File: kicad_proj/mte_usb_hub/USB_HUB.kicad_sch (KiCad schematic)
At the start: 50 parts

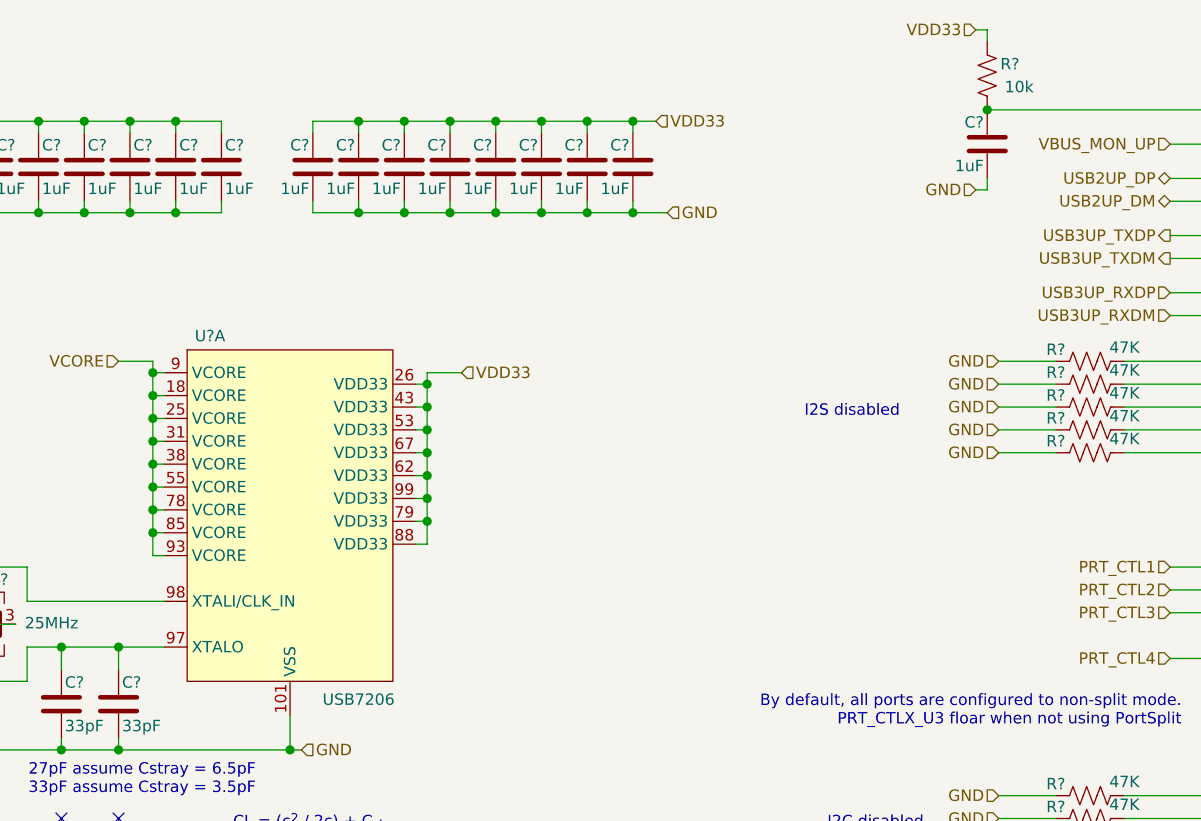
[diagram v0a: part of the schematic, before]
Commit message: Finishes upstream USB setup
No power setup, no downstream ports setup
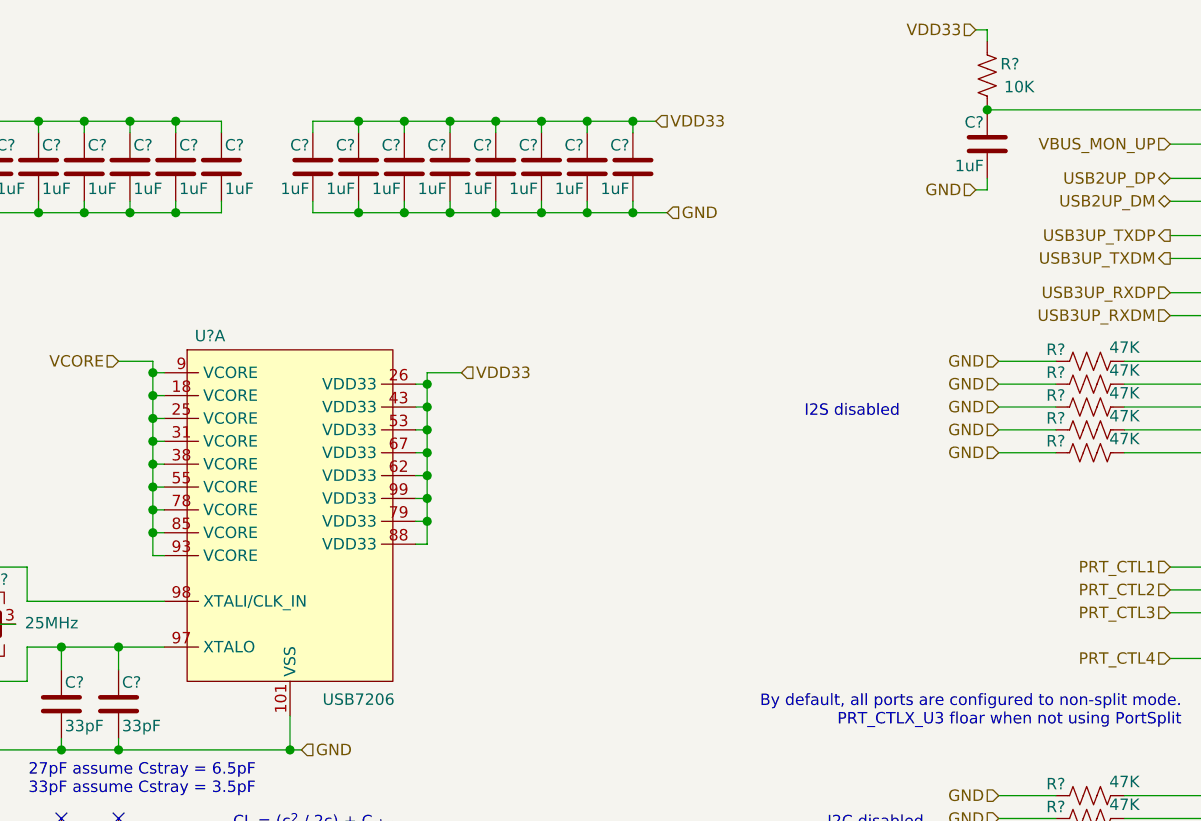
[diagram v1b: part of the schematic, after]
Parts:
- C? (x18): symbol capacitors:CC0402KRX5R7BB105 -> mte_usb_hub:CC0402KRX5R7BB105
- C? (x2): symbol capacitors:CC0402JRNPO9BN330 -> mte_usb_hub:CC0402JRNPO9BN330
- C? (x2): symbol capacitors:CC0402JRNPO9BN270 -> mte_usb_hub:CC0402JRNPO9BN270
- R? (x13): symbol resistors:RC0402JR-0747KL -> mte_usb_hub:RC0402JR-0747KL
- R? (x7): symbol resistors:RC0402JR-0710KL -> mte_usb_hub:RC0402JR-0710KL
- R?: symbol resistors:RC0402JR-0710KL -> mte_usb_hub:RC0402JR-0710KL; id 10k -> 10K

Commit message: Final tweaks for the video
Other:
- moved on the sheet: C?, Y?

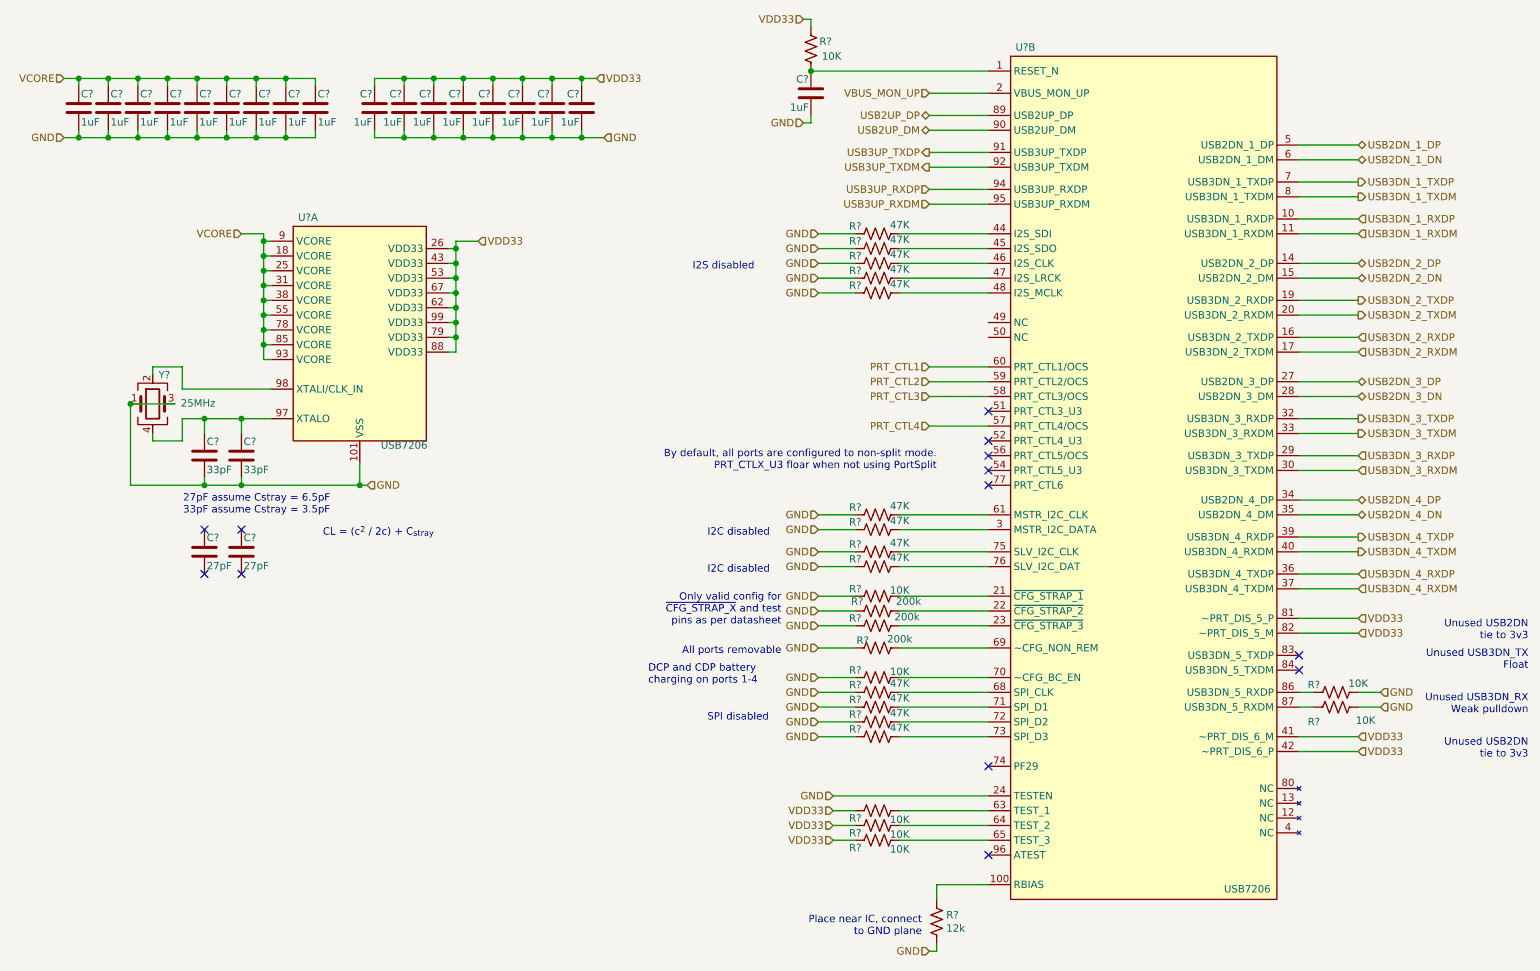
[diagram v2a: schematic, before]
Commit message: Updates input protection, output BC enabled
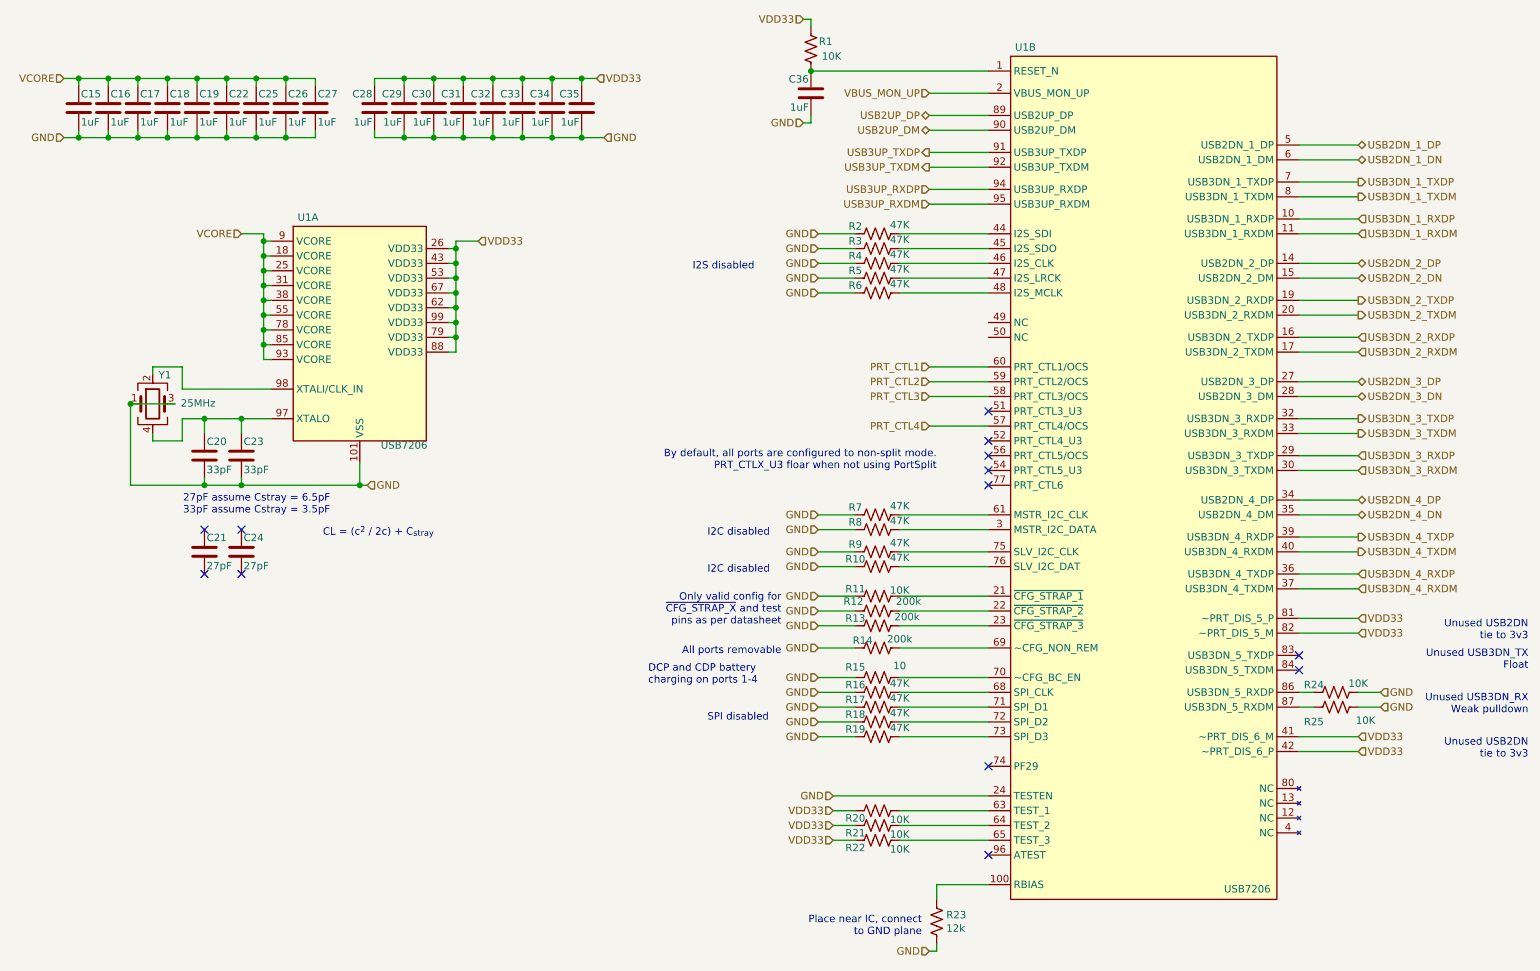
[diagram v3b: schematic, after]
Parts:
- removed R?: RC0402JR-0710KL, footprints:RESISTOR_0402N, symbol mte_usb_hub:RC0402JR-0710KL
- added R15: RC0402JR-0710RL, footprints:RESISTOR_0402N, symbol mte_usb_hub:RC0402JR-0710RL
- gave numbers to parts that had none: 48
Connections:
- net GND: now also R15.1
- net at U1.70 (PF22): now also R15.2

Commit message: New changes from the livestream
Starts the layout
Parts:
- C15, C16, C17, C18, C19, C20, C21, C22, C23, C24, C25, C26, C27, C28, C29, C30, C31, C32, C33, C34, C35, C36: footprint footprints:CAPACITOR_0402N -> mte_usb_footprints:CAPACITOR_0402N
- R1, R10, R11, R12, R13, R14, R15, R16, R17, R18, R19, R2, R20, R21, R22, R23, R24, R25, R3, R4, R5, R6, R7, R8, R9: footprint footprints:RESISTOR_0402N -> mte_usb_footprints:RESISTOR_0402N
- U1: footprint (none) -> mte_usb_footprints:QFN101P40_1200X1200X90L60X20T800N
- Y1: footprint footprints:RH100-12.000-10-2020-EXT-TR -> mte_usb_footprints:RH100-12.000-10-2020-EXT-TR
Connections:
- net USB2UP_DM renamed USB2UP_DN
- net USB3DN_1_RXDM renamed USB3DN_1_RXDN
- net USB3DN_1_TXDM renamed USB3DN_1_TXDN
- net USB3DN_2_RXDM renamed USB3DN_2_RXDN
- net USB3DN_2_TXDM renamed USB3DN_2_TXDN
- net USB3DN_3_RXDM renamed USB3DN_3_RXDN
- net USB3DN_3_TXDM renamed USB3DN_3_TXDN
- net USB3DN_4_RXDM renamed USB3DN_4_RXDN
- net USB3DN_4_TXDM renamed USB3DN_4_TXDN
- net USB3UP_RXDM renamed USB3UP_RXDN
- net USB3UP_TXDM renamed USB3UP_TXDN

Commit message: Updates from the livestream
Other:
- note added: "Only valid config for ~{CFG_STRAP_X and test pins as per datasheet}"
- note removed: "Only valid config for ~CFG_STRAP_X and test pins as per datasheet"
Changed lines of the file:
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@@
-(kicad_sch (version 20210406) (generator eeschema)
+(kicad_sch (version 20210606) (generator eeschema)
   (paper "A4")
   (junction (at 22.86 24.13) (diameter 1.016) (color 0 0 0 0))
@@
     (effects (font (size 1.27 1.27)) (justify left bottom))
   )
-  (text "Only valid config for \n~CFG_STRAP_X and test\npins as per datasheet"
+  (text "Only valid config for \n~{CFG_STRAP_X and test\npins as per datasheet}"
     (at 143.51 118.11 0)
     (effects (font (size 1.27 1.27)) (justify right bottom))

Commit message: Updates from the livestream
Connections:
- net at C20.1, U1.97 (XTALO), Y1.4: no longer C23.1
- net at U1.98 (XTALI/CLK_IN), Y1.2: now also C23.1
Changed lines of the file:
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@@
   (junction (at 48.26 24.13) (diameter 1.016) (color 0 0 0 0))
   (junction (at 48.26 34.29) (diameter 1.016) (color 0 0 0 0))
-  (junction (at 50.8 82.55) (diameter 1.016) (color 0 0 0 0))
   (junction (at 50.8 93.98) (diameter 1.016) (color 0 0 0 0))
   (junction (at 53.34 24.13) (diameter 1.016) (color 0 0 0 0))
   (junction (at 53.34 34.29) (diameter 1.016) (color 0 0 0 0))
+  (junction (at 53.34 77.47) (diameter 1.016) (color 0 0 0 0))
   (junction (at 54.61 52.07) (diameter 1.016) (color 0 0 0 0))
   (junction (at 54.61 54.61) (diameter 1.016) (color 0 0 0 0))
@@
     (stroke (width 0) (type solid) (color 0 0 0 0))
   )
-  (wire (pts (xy 40.64 77.47) (xy 55.88 77.47))
+  (wire (pts (xy 40.64 77.47) (xy 53.34 77.47))
     (stroke (width 0) (type solid) (color 0 0 0 0))
   )
@@
     (stroke (width 0) (type solid) (color 0 0 0 0))
   )
-  (wire (pts (xy 44.45 82.55) (xy 50.8 82.55))
+  (wire (pts (xy 44.45 82.55) (xy 55.88 82.55))
     (stroke (width 0) (type solid) (color 0 0 0 0))
   )
@@
     (stroke (width 0) (type solid) (color 0 0 0 0))
   )
-  (wire (pts (xy 50.8 82.55) (xy 50.8 85.09))
-    (stroke (width 0) (type solid) (color 0 0 0 0))
-  )
-  (wire (pts (xy 50.8 82.55) (xy 55.88 82.55))
+  (wire (pts (xy 50.8 83.82) (xy 53.34 81.28))
+    (stroke (width 0) (type solid) (color 0 0 0 0))
+  )
+  (wire (pts (xy 50.8 85.09) (xy 50.8 83.82))
     (stroke (width 0) (type solid) (color 0 0 0 0))
   )
@@
     (stroke (width 0) (type solid) (color 0 0 0 0))
   )
+  (wire (pts (xy 53.34 77.47) (xy 55.88 77.47))
+    (stroke (width 0) (type solid) (color 0 0 0 0))
+  )
+  (wire (pts (xy 53.34 81.28) (xy 53.34 77.47))
+    (stroke (width 0) (type solid) (color 0 0 0 0))
+  )
